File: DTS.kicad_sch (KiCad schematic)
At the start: 0 parts

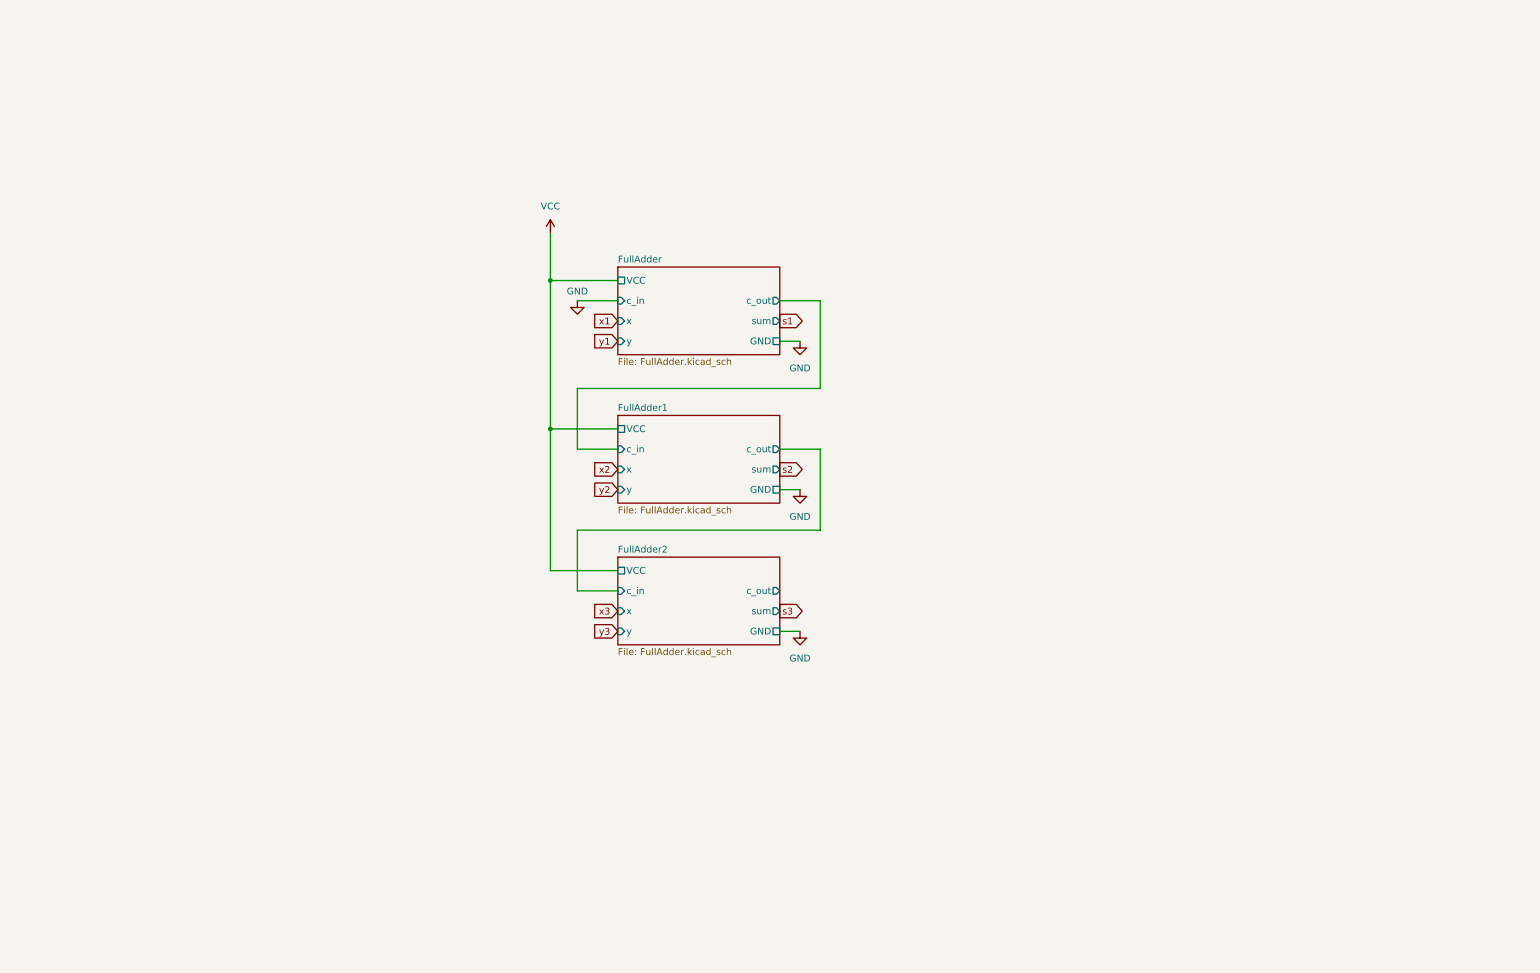
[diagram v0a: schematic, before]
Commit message: Add files via upload
Added 3 bits 2:1 and 6 bits 4:1 multiplexer
Added minus operation
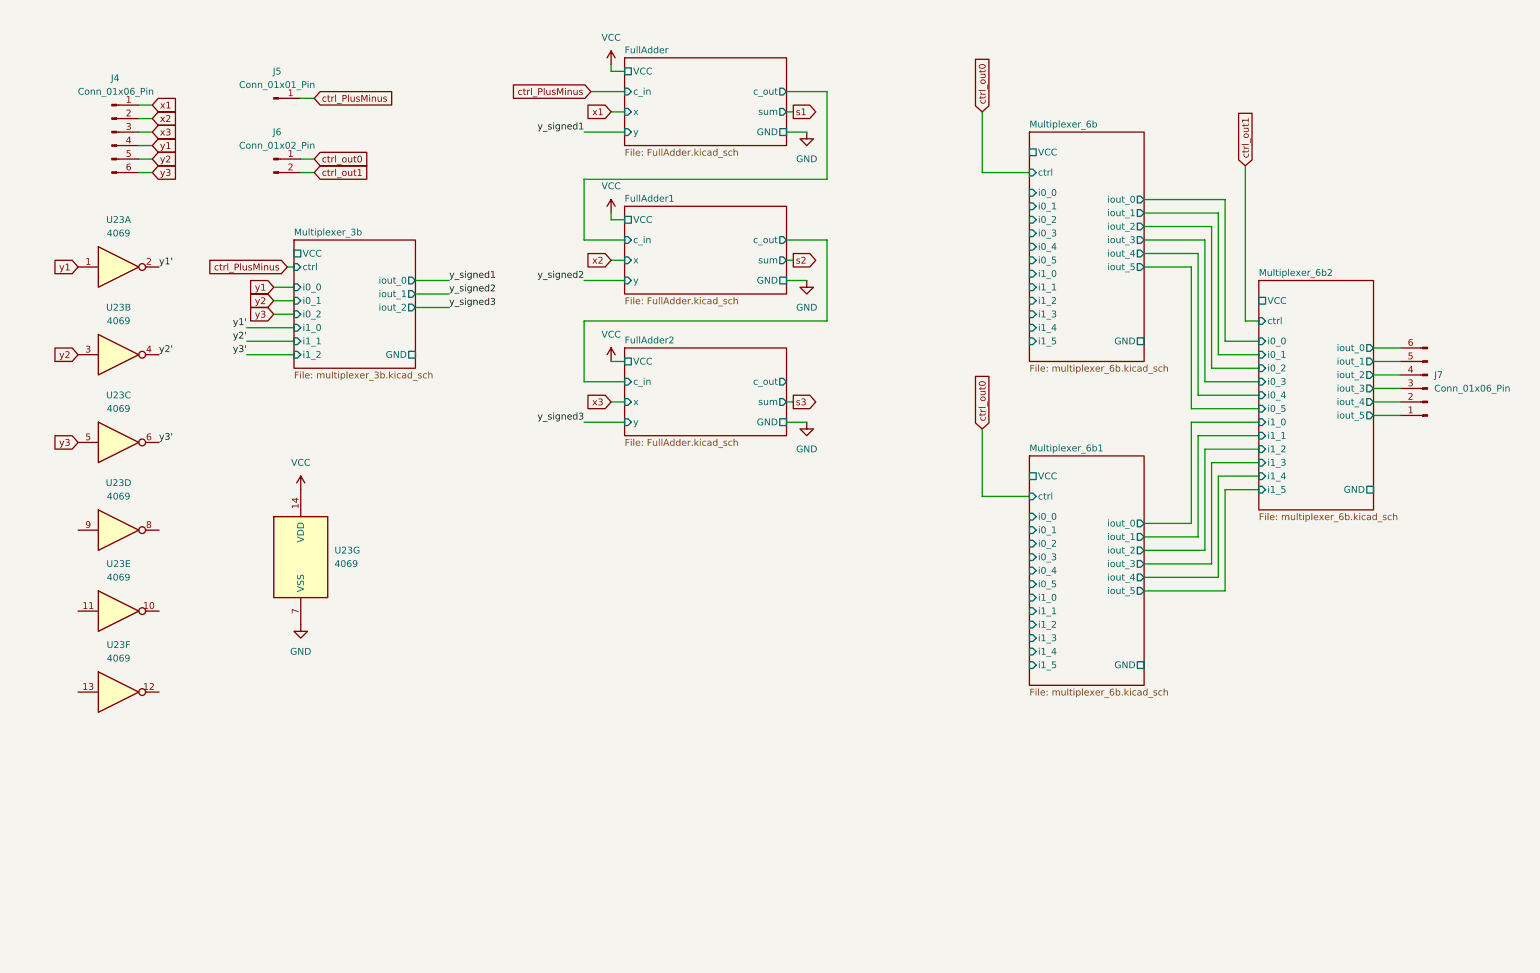
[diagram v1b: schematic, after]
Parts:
- added J4, J7: Conn_01x06_Pin, symbol Connector:Conn_01x06_Pin
- added J5: Conn_01x01_Pin, symbol Connector:Conn_01x01_Pin
- added J6: Conn_01x02_Pin, symbol Connector:Conn_01x02_Pin
- added U23: 4069, symbol 4xxx:4069
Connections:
- net GND: now also U23.7 (VSS)
- net VCC: now also U23.14 (VDD)
- net x1: now also J4.1 (Pin_1)
- net x2: now also J4.2 (Pin_2)
- net x3: now also J4.3 (Pin_3)
- net y1: now also J4.4 (Pin_4), U23.1
- net y2: now also J4.5 (Pin_5), U23.3
- net y3: now also J4.6 (Pin_6), U23.5
- new net Multiplexer_6b2/iout_0: J7.6 (Pin_6)
- new net Multiplexer_6b2/iout_1: J7.5 (Pin_5)
- new net Multiplexer_6b2/iout_2: J7.4 (Pin_4)
- new net Multiplexer_6b2/iout_3: J7.3 (Pin_3)
- new net Multiplexer_6b2/iout_4: J7.2 (Pin_2)
- new net Multiplexer_6b2/iout_5: J7.1 (Pin_1)
- new net ctrl_PlusMinus: J5.1 (Pin_1)
- new net ctrl_out0: J6.1 (Pin_1)
- new net ctrl_out1: J6.2 (Pin_2)
- new net y1': U23.2
- new net y2': U23.4
- new net y3': U23.6
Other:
- added sheet Multiplexer_3b (multiplexer_3b.kicad_sch)
- added sheet Multiplexer_6b (multiplexer_6b.kicad_sch)
- added sheet Multiplexer_6b1 (multiplexer_6b.kicad_sch)
- added sheet Multiplexer_6b2 (multiplexer_6b.kicad_sch)

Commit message: Add files via upload
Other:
- added sheet Multiplier (multiplier.kicad_sch)
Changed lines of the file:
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@@
+	)
+	(sheet
+		(at 130.81 113.03)
+		(size 26.67 24.13)
+		(exclude_from_sim no)
+		(in_bom yes)
+		(on_board yes)
+		(dnp no)
+		(fields_autoplaced yes)
+		(stroke
+			(width 0.1524)
+			(type solid)
+		)
+		(fill
+			(color 0 0 0 0.0000)
+		)
+		(property "Sheetname" "Multiplier"
+			(at 130.81 112.3184 0)
+			(effects
+				(font
+					(size 1.27 1.27)
+				)
+				(justify left bottom)
+			)
+		)
+		(property "Sheetfile" "multiplier.kicad_sch"
+			(at 130.81 137.7446 0)
+			(effects
+				(font
+					(size 1.27 1.27)
+				)
+				(justify left top)
+			)
+		)
+		(pin "A0" input
+			(at 130.81 115.57 180)
+			(effects
+				(font
+					(size 1.27 1.27)
+				)
+				(justify left)
+			)
+		)
+		(pin "A1" input
+			(at 130.81 119.38 180)
+			(effects
+				(font
+					(size 1.27 1.27)
+				)
+				(justify left)
+			)
+		)
+		(pin "A2" input
+			(at 130.81 123.19 180)
+			(effects
+				(font
+					(size 1.27 1.27)
+				)
+				(justify left)
+			)
+		)
+		(pin "B0" input
+			(at 130.81 127 180)
+			(effects
+				(font
+					(size 1.27 1.27)
+				)
+				(justify left)
+			)
+		)
+		(pin "B1" input
+			(at 130.81 130.81 180)
+			(effects
+				(font
+					(size 1.27 1.27)
+				)
+				(justify left)
+			)
+		)
+		(pin "B2" input
+			(at 130.81 134.62 180)
+			(effects
+				(font
+					(size 1.27 1.27)
+				)
+				(justify left)
+			)
+		)
+		(pin "OUT0" output
+			(at 157.48 115.57 0)
+			(effects
+				(font
+					(size 1.27 1.27)
+				)
+				(justify right)
+			)
+		)
+		(pin "OUT1" output
+			(at 157.48 119.38 0)
+			(effects
+				(font
+					(size 1.27 1.27)
+				)
+				(justify right)
+			)
+		)
+		(pin "OUT2" output
+			(at 157.48 123.19 0)
+			(effects
+				(font
+					(size 1.27 1.27)
+				)
+				(justify right)
+			)
+		)
+		(pin "OUT3" output
+			(at 157.48 127 0)
+			(effects
+				(font
+					(size 1.27 1.27)
+				)
+				(justify right)
+			)
+		)
+		(pin "OUT4" output
+			(at 157.48 130.81 0)
+			(effects
+				(font
+					(size 1.27 1.27)
+				)
+				(justify right)
+			)
+		)
+		(pin "OUT5" output
+			(at 157.48 134.62 0)
+			(effects
+				(font
+					(size 1.27 1.27)
+				)
+				(justify right)
+			)
+		)
+		(instances
+			(project "DTS"
+				(path "/1bd2ca98-343e-4f04-8d6c-1f7257d9e9fe"
+					(page "9")
+				)
+			)
+		)
 	)
 	(sheet

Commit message: Add files via upload
Waiting for approval
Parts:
- removed J5: Conn_01x01_Pin, symbol Connector:Conn_01x01_Pin
- added C1: 0.22u, symbol Device:C
- added C2: 0.1u, symbol Device:C
- added J5: Conn_01x02_Pin, symbol Connector:Conn_01x02_Pin
- added SW1: SW_DIP_x01, symbol Switch:SW_DIP_x01
- added U69: LM7805_TO220, Package_TO_SOT_THT:TO-220-3_Vertical, symbol Regulator_Linear:LM7805_TO220
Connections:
- net GND: now also C1.2, C2.2, J5.2 (Pin_2), U69.2 (GND)
- net VCC: now also C2.1, U69.3 (VO)
- new net: J5.1 (Pin_1), SW1.1
- new net: C1.1, SW1.2, U69.1 (VI)
- no-connect marks 0 -> 4
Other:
- added sheet Signed_Extended (Signed_Extended.kicad_sch)
- sheet FullAdder ports: added xor_out; removed none
- sheet FullAdder1 ports: added xor_out; removed none
- sheet FullAdder2 ports: added xor_out; removed none
- note added: "ADDER"
- note added: "INPUT PIN"
- note added: "POWER"
- note added: "SIGN EXTEND"
- note added: "TWO'S COMPLIMENT"
- moved on the sheet: U23A, U23B, U23C, U23D, U23E, U23F, U23G
